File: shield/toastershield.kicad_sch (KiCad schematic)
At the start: 27 parts, among them J1 Power, J2 Digital/PWM, J3 Analog, J4 Digital/PWM, SW1 SW_SPDT, SW2 SW_SPDT, SW3 SW_SPDT, SW4 SW_SPDT, U2 NE555P, U3 74HC14

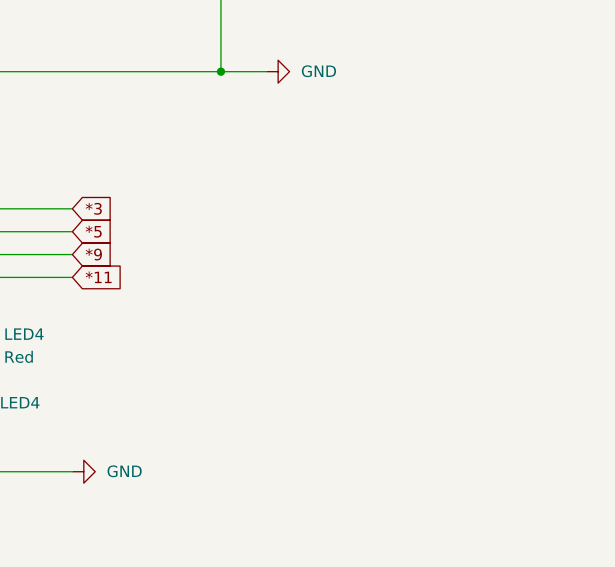
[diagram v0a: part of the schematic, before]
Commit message: feat: i2c pullups on the shield
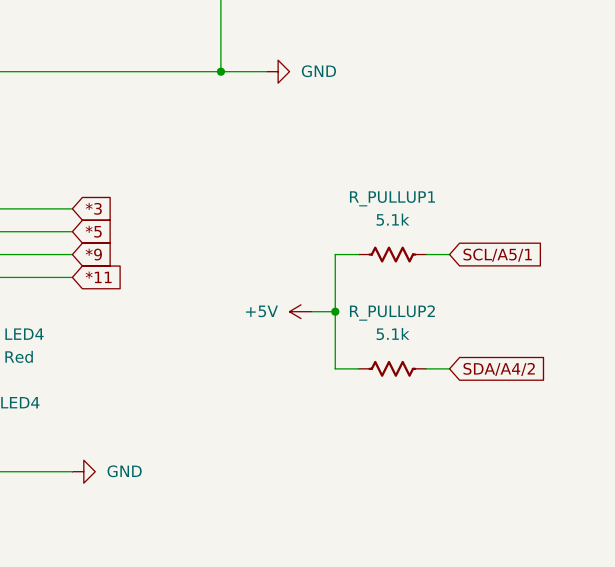
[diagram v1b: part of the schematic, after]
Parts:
- added R_PULLUP1, R_PULLUP2: 5.1k, PCM_Resistor_THT_US_AKL:R_Axial_DIN0207_L6.3mm_D2.5mm_P2.54mm_Vertical, symbol PCM_Resistor_US_AKL:R_DIN0207_P5.08mm
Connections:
- net +5V: now also R_PULLUP1.1, R_PULLUP2.1
- net SCL/A5/1: now also R_PULLUP1.2
- net SDA/A4/2: now also R_PULLUP2.2
